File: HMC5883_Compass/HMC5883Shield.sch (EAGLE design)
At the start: 7 parts

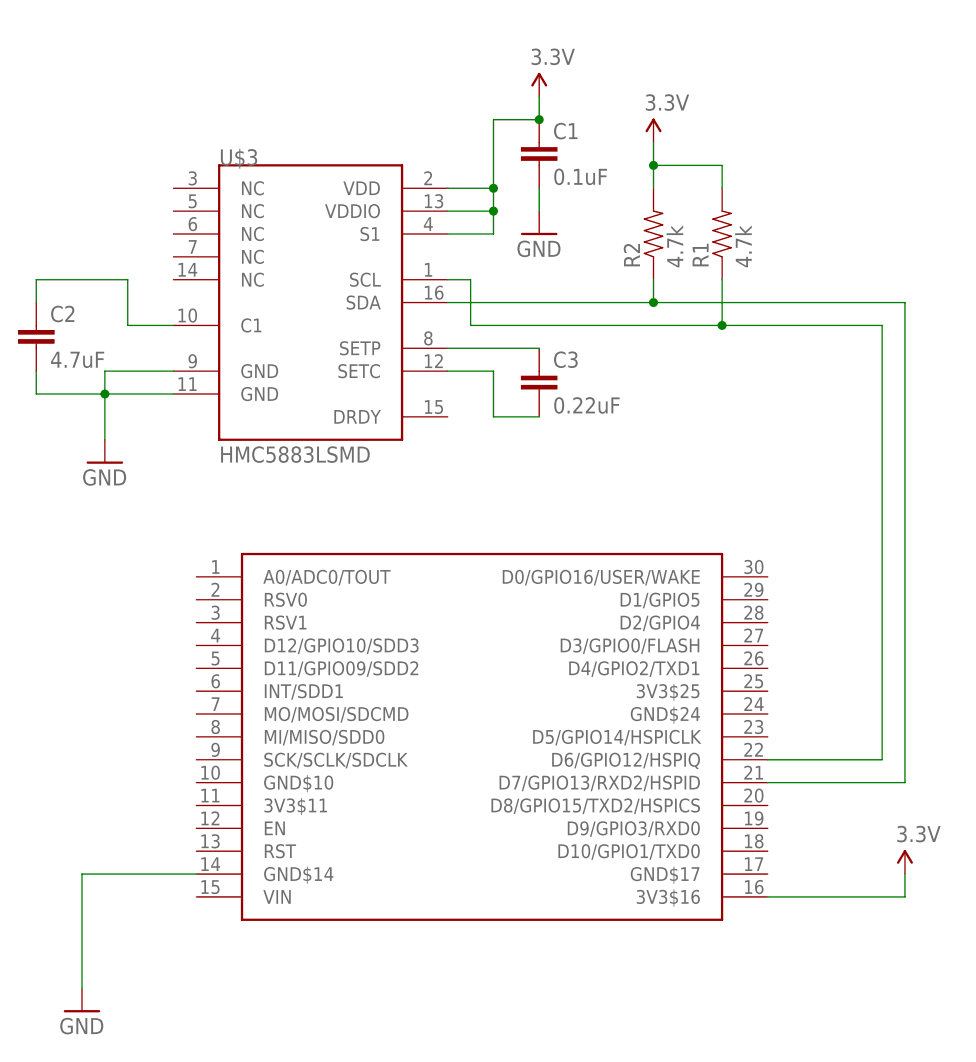
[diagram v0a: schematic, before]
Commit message: Added OLED Shield Added LiPo Battery Charger Shield Updated outlines of all shields to match the cutout of the nodemcu board
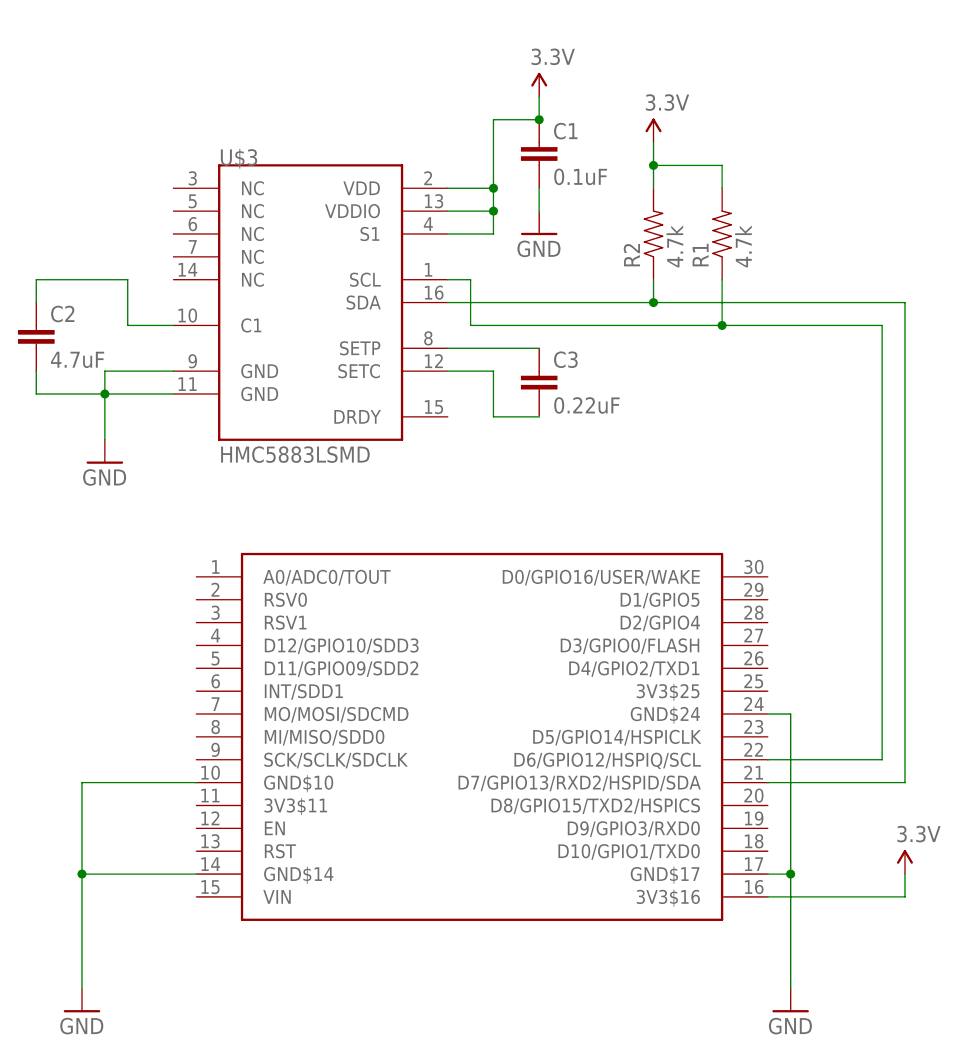
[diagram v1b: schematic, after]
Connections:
- net GND: now also U$1.GND$10, U$1.GND$17, U$1.GND$24
- net N$2: now also U$1.D7/GPIO13/RXD2/HSPID/SDA; no longer U$1.D7/GPIO13/RXD2/HSPID
- net N$3: now also U$1.D6/GPIO12/HSPIQ/SCL; no longer U$1.D6/GPIO12/HSPIQ
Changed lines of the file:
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@@
 <?xml version="1.0" encoding="utf-8"?>
 <!DOCTYPE eagle SYSTEM "eagle.dtd">
-<eagle version="7.3.0">
+<eagle version="7.4.0">
 <drawing>
 <settings>
@@
 <part name="GND3" library="SparkFun" deviceset="GND" device=""/>
 <part name="C3" library="SparkFun" deviceset="CAP" device="0402-CAP" value="0.22uF"/>
+<part name="GND4" library="SparkFun" deviceset="GND" device=""/>
 </parts>
 <sheets>
@@
 <instance part="GND3" gate="1" x="45.72" y="104.14"/>
 <instance part="C3" gate="G$1" x="45.72" y="86.36"/>
+<instance part="GND4" gate="1" x="73.66" y="17.78"/>
 </instances>
 <busses>
@@
 <wire x1="7.62" y1="33.02" x2="-5.08" y2="33.02" width="0.1524" layer="91"/>
 <wire x1="-5.08" y1="33.02" x2="-5.08" y2="20.32" width="0.1524" layer="91"/>
+<pinref part="U$1" gate="G$1" pin="GND$10"/>
+<wire x1="7.62" y1="43.18" x2="-5.08" y2="43.18" width="0.1524" layer="91"/>
+<wire x1="-5.08" y1="43.18" x2="-5.08" y2="33.02" width="0.1524" layer="91"/>
+<junction x="-5.08" y="33.02"/>
 </segment>
 <segment>
@@
 <pinref part="GND3" gate="1" pin="GND"/>
 <wire x1="45.72" y1="109.22" x2="45.72" y2="106.68" width="0.1524" layer="91"/>
+</segment>
+<segment>
+<pinref part="U$1" gate="G$1" pin="GND$17"/>
+<pinref part="GND4" gate="1" pin="GND"/>
+<wire x1="71.12" y1="33.02" x2="73.66" y2="33.02" width="0.1524" layer="91"/>
+<wire x1="73.66" y1="33.02" x2="73.66" y2="20.32" width="0.1524" layer="91"/>
+<pinref part="U$1" gate="G$1" pin="GND$24"/>
+<wire x1="71.12" y1="50.8" x2="73.66" y2="50.8" width="0.1524" layer="91"/>
+<wire x1="73.66" y1="50.8" x2="73.66" y2="33.02" width="0.1524" layer="91"/>
+<junction x="73.66" y="33.02"/>
 </segment>
 </net>
@@
 <wire x1="86.36" y1="96.52" x2="86.36" y2="43.18" width="0.1524" layer="91"/>
 <junction x="58.42" y="96.52"/>
-<pinref part="U$1" gate="G$1" pin="D7/GPIO13/RXD2/HSPID"/>
+<pinref part="U$1" gate="G$1" pin="D7/GPIO13/RXD2/HSPID/SDA"/>
 <wire x1="86.36" y1="43.18" x2="71.12" y2="43.18" width="0.1524" layer="91"/>
 <wire x1="58.42" y1="96.52" x2="35.56" y2="96.52" width="0.1524" layer="91"/>
@@
 <wire x1="83.82" y1="93.98" x2="83.82" y2="45.72" width="0.1524" layer="91"/>
 <junction x="66.04" y="93.98"/>
-<pinref part="U$1" gate="G$1" pin="D6/GPIO12/HSPIQ"/>
+<pinref part="U$1" gate="G$1" pin="D6/GPIO12/HSPIQ/SCL"/>
 <wire x1="83.82" y1="45.72" x2="71.12" y2="45.72" width="0.1524" layer="91"/>
 <wire x1="38.1" y1="93.98" x2="38.1" y2="99.06" width="0.1524" layer="91"/>

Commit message: Updated the i2c pins to all shields to use d11/d12  as these pins will have dual use with the upcoming wifimcu Added FM24W256  Fram shield Added X95840 Digital potentiometer Shield Added AD5696 DAC Shield
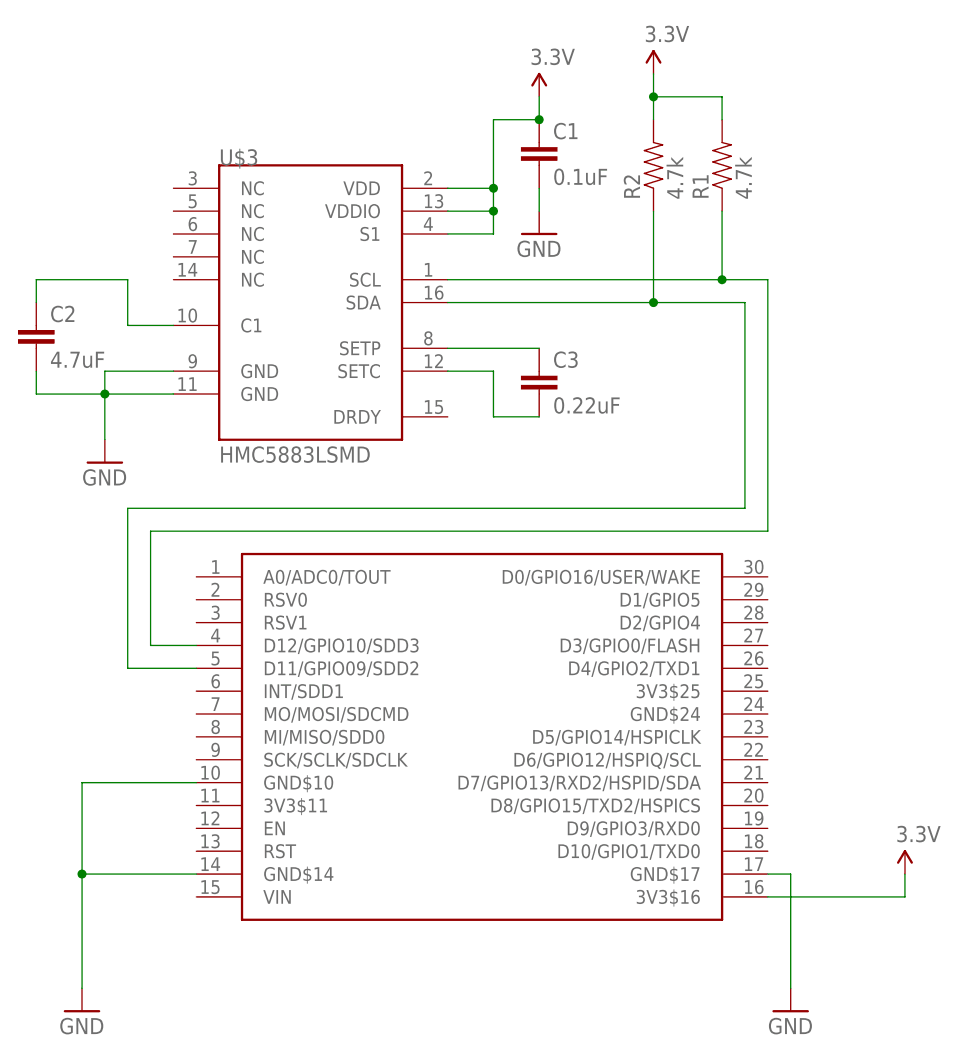
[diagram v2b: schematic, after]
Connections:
- net GND: no longer U$1.GND$24
- net N$2: now also U$1.D11/GPIO09/SDD2; no longer U$1.D7/GPIO13/RXD2/HSPID/SDA
- net N$3: now also U$1.D12/GPIO10/SDD3; no longer U$1.D6/GPIO12/HSPIQ/SCL
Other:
- moved on the sheet: R1, R2
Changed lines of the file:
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@@
 <instance part="P+1" gate="G$1" x="86.36" y="33.02"/>
 <instance part="P+2" gate="G$1" x="45.72" y="119.38"/>
-<instance part="R1" gate="G$1" x="66.04" y="104.14" rot="R90"/>
-<instance part="R2" gate="G$1" x="58.42" y="104.14" rot="R90"/>
+<instance part="R1" gate="G$1" x="66.04" y="111.76" rot="R90"/>
+<instance part="R2" gate="G$1" x="58.42" y="111.76" rot="R90"/>
 <instance part="C1" gate="G$1" x="45.72" y="111.76"/>
-<instance part="P+3" gate="G$1" x="58.42" y="114.3"/>
+<instance part="P+3" gate="G$1" x="58.42" y="121.92"/>
 <instance part="U$3" gate="G$1" x="20.32" y="96.52"/>
 <instance part="C2" gate="G$1" x="-10.16" y="91.44"/>
@@
 <wire x1="71.12" y1="33.02" x2="73.66" y2="33.02" width="0.1524" layer="91"/>
 <wire x1="73.66" y1="33.02" x2="73.66" y2="20.32" width="0.1524" layer="91"/>
-<pinref part="U$1" gate="G$1" pin="GND$24"/>
-<wire x1="71.12" y1="50.8" x2="73.66" y2="50.8" width="0.1524" layer="91"/>
-<wire x1="73.66" y1="50.8" x2="73.66" y2="33.02" width="0.1524" layer="91"/>
-<junction x="73.66" y="33.02"/>
 </segment>
 </net>
@@
 <pinref part="R2" gate="G$1" pin="2"/>
 <pinref part="P+3" gate="G$1" pin="3.3V"/>
-<wire x1="58.42" y1="109.22" x2="58.42" y2="111.76" width="0.1524" layer="91"/>
+<wire x1="58.42" y1="116.84" x2="58.42" y2="119.38" width="0.1524" layer="91"/>
 <pinref part="R1" gate="G$1" pin="2"/>
-<wire x1="58.42" y1="111.76" x2="58.42" y2="114.3" width="0.1524" layer="91"/>
-<wire x1="66.04" y1="109.22" x2="66.04" y2="111.76" width="0.1524" layer="91"/>
-<wire x1="66.04" y1="111.76" x2="58.42" y2="111.76" width="0.1524" layer="91"/>
-<junction x="58.42" y="111.76"/>
+<wire x1="58.42" y1="119.38" x2="58.42" y2="121.92" width="0.1524" layer="91"/>
+<wire x1="66.04" y1="116.84" x2="66.04" y2="119.38" width="0.1524" layer="91"/>
+<wire x1="66.04" y1="119.38" x2="58.42" y2="119.38" width="0.1524" layer="91"/>
+<junction x="58.42" y="119.38"/>
 </segment>
 </net>
@@
 <segment>
 <pinref part="R2" gate="G$1" pin="1"/>
-<wire x1="58.42" y1="96.52" x2="58.42" y2="99.06" width="0.1524" layer="91"/>
-<wire x1="58.42" y1="96.52" x2="86.36" y2="96.52" width="0.1524" layer="91"/>
-<wire x1="86.36" y1="96.52" x2="86.36" y2="43.18" width="0.1524" layer="91"/>
+<wire x1="58.42" y1="96.52" x2="58.42" y2="106.68" width="0.1524" layer="91"/>
+<wire x1="58.42" y1="96.52" x2="68.58" y2="96.52" width="0.1524" layer="91"/>
+<wire x1="68.58" y1="96.52" x2="68.58" y2="73.66" width="0.1524" layer="91"/>
 <junction x="58.42" y="96.52"/>
-<pinref part="U$1" gate="G$1" pin="D7/GPIO13/RXD2/HSPID/SDA"/>
-<wire x1="86.36" y1="43.18" x2="71.12" y2="43.18" width="0.1524" layer="91"/>
 <wire x1="58.42" y1="96.52" x2="35.56" y2="96.52" width="0.1524" layer="91"/>
 <pinref part="U$3" gate="G$1" pin="SDA"/>
+<wire x1="68.58" y1="73.66" x2="0" y2="73.66" width="0.1524" layer="91"/>
+<wire x1="0" y1="73.66" x2="0" y2="55.88" width="0.1524" layer="91"/>
+<pinref part="U$1" gate="G$1" pin="D11/GPIO09/SDD2"/>
+<wire x1="0" y1="55.88" x2="7.62" y2="55.88" width="0.1524" layer="91"/>
 </segment>
 </net>
@@
 <segment>
 <pinref part="R1" gate="G$1" pin="1"/>
-<wire x1="38.1" y1="93.98" x2="66.04" y2="93.98" width="0.1524" layer="91"/>
-<wire x1="66.04" y1="93.98" x2="66.04" y2="99.06" width="0.1524" layer="91"/>
-<wire x1="66.04" y1="93.98" x2="83.82" y2="93.98" width="0.1524" layer="91"/>
-<wire x1="83.82" y1="93.98" x2="83.82" y2="45.72" width="0.1524" layer="91"/>
-<junction x="66.04" y="93.98"/>
-<pinref part="U$1" gate="G$1" pin="D6/GPIO12/HSPIQ/SCL"/>
-<wire x1="83.82" y1="45.72" x2="71.12" y2="45.72" width="0.1524" layer="91"/>
-<wire x1="38.1" y1="93.98" x2="38.1" y2="99.06" width="0.1524" layer="91"/>
+<wire x1="35.56" y1="99.06" x2="66.04" y2="99.06" width="0.1524" layer="91"/>
+<wire x1="66.04" y1="99.06" x2="66.04" y2="106.68" width="0.1524" layer="91"/>
+<wire x1="66.04" y1="99.06" x2="71.12" y2="99.06" width="0.1524" layer="91"/>
+<wire x1="71.12" y1="99.06" x2="71.12" y2="71.12" width="0.1524" layer="91"/>
+<junction x="66.04" y="99.06"/>
 <pinref part="U$3" gate="G$1" pin="SCL"/>
-<wire x1="38.1" y1="99.06" x2="35.56" y2="99.06" width="0.1524" layer="91"/>
+<wire x1="71.12" y1="71.12" x2="2.54" y2="71.12" width="0.1524" layer="91"/>
+<wire x1="2.54" y1="71.12" x2="2.54" y2="58.42" width="0.1524" layer="91"/>
+<pinref part="U$1" gate="G$1" pin="D12/GPIO10/SDD3"/>
+<wire x1="2.54" y1="58.42" x2="7.62" y2="58.42" width="0.1524" layer="91"/>
 </segment>
 </net>
